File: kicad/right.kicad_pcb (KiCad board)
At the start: 4 copper layers, 127.3 x 89.6 mm, 150 parts, among them Q1 PMF170XP,115, Q2 FS8205A_C2830320, SW1 TS-1088-AR02016, U1 TLV7031QDCKRQ1, U2 E73-2G4M08S1C, U3 SN74LVC1G74DQER, U4 BL8573CS8TR, U6 S2B-PH-K-S(LF)(SN), U7 LP5024RSMR, U8 DW01A_C42380662, X1 FC-13532.768KHZ9PF20PPM

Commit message: added fiducials
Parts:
- added ?: , , F.Cu at (25.4, 113.4)
- added ?: , , B.Cu at (25.4, 113.4)
- added ?: , , B.Cu at (152.4, 49.0)
- added ?: , , B.Cu at (25.4, 49.0)
- added REF**: Fiducial_1mm_Mask2mm, Fiducial:Fiducial_1mm_Mask2mm, F.Cu at (152.4, 49.0)
- added REF**: Fiducial_1mm_Mask2mm, Fiducial:Fiducial_1mm_Mask2mm, F.Cu at (25.4, 49.0)
- moved G** 261.5 mm to (370.8, 131.0)
- moved G*** 237.1 mm to (390.8, -23.2)
- moved G*** 237.1 mm to (401.2, 64.9)
- moved Battery? 71.2 mm to (58.6, 75.3)
- moved C6 71.2 mm to (145.7, 42.9)
- moved C7 71.2 mm to (145.7, 64.4)
- moved C8 71.2 mm to (145.7, 85.9)
- moved D2 71.2 mm to (152.8, 51.1)
- moved D3 71.2 mm to (152.8, 72.6)
- moved D4 71.2 mm to (152.8, 94.1)
- moved D5 71.2 mm to (134.0, 40.3)
- moved D6 71.2 mm to (134.0, 61.8)
- moved D7 71.2 mm to (134.0, 83.3)
- moved hex_edge 71.2 mm to (144.6, 91.9)
- moved hex_edge 71.2 mm to (144.6, 48.9)
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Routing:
- net /D+: track 77.8 -> 71.3 mm
- net /D-: track 73.1 -> 69.0 mm
- net /LED20: track 43.9 -> 45.7 mm

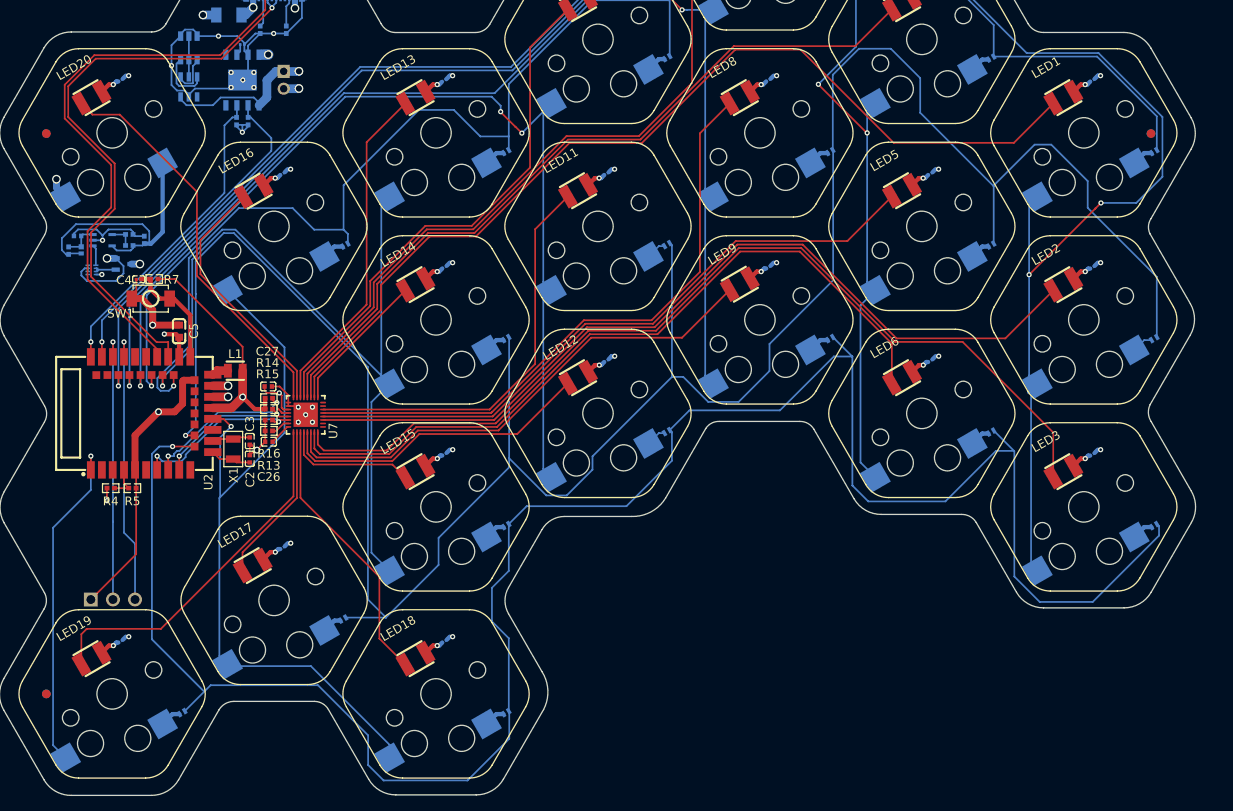
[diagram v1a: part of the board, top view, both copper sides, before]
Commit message: added mounting holes
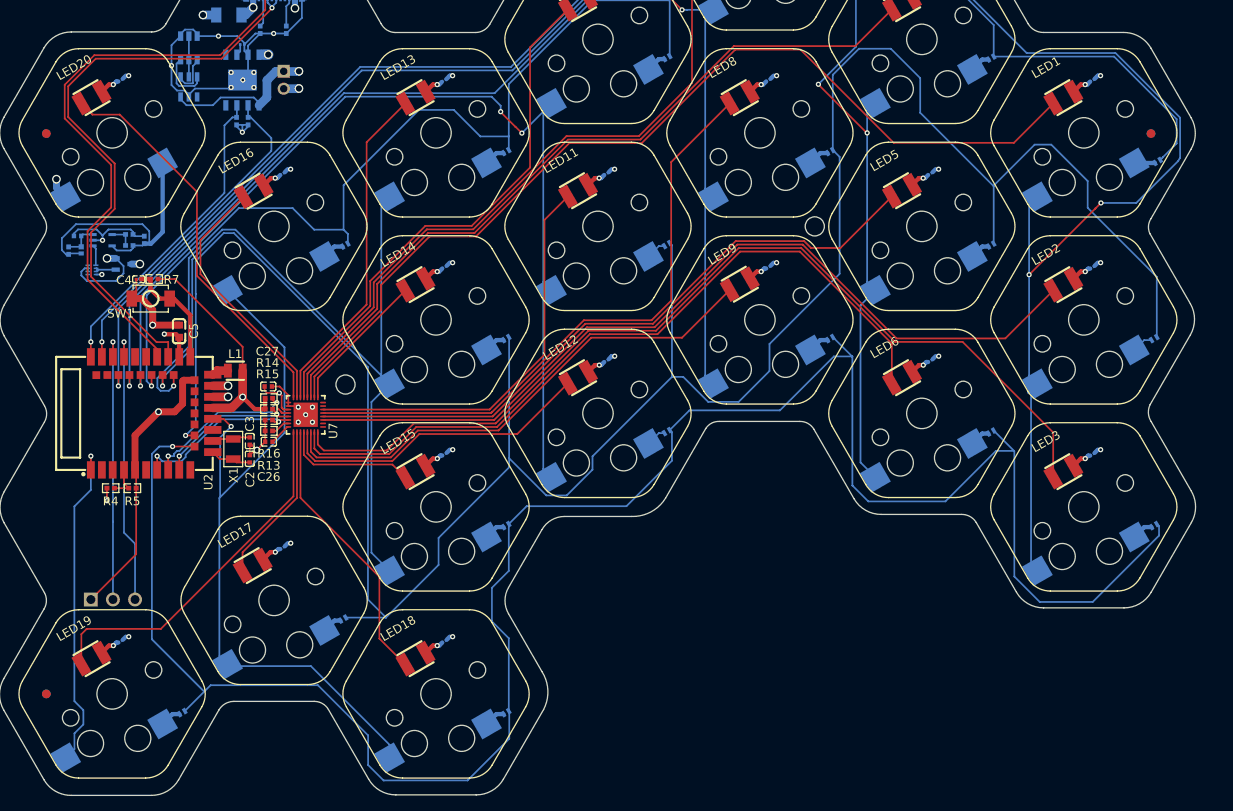
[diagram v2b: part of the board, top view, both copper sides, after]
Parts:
- added ?: , , F.Cu at (59.8, 77.8)
- added M2: MountingHole_2.2mm_M2, MountingHole:MountingHole_2.2mm_M2, F.Cu at (113.8, 59.7)
- Fi1, Fi2, Fi3, Fi6: renamed from ?; value (none) -> Fiducial_1mm_Mask2mm
- moved D2 1.20 mm to (153.2, 52.2)
- renumbered REF** to Fi4, REF** to Fi5
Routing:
- net /ROW1: track 183.0 -> 187.0 mm
- net /COL1: track 230.7 -> 233.5 mm
- net /LED5: track 75.9 -> 76.5 mm
- net /ROW2: track 286.0 -> 286.6 mm

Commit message: changed mounting holes. cleared a little bit, created 21 key version... needs 21 key integration
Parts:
- removed the ? at (59.8, 77.8)
- removed the S12 at (88.9, 102.7)
- added REF**: MountingHole_2.2mm_M2, MountingHole:MountingHole_2.2mm_M2, F.Cu at (57.8, 38.2)
- added REF**: MountingHole_2.2mm_M2, MountingHole:MountingHole_2.2mm_M2, F.Cu at (40.7, 91.9)
- added hex_edge: , clipboard:b9cf7df6-7b49-4194-bf11-16aaca528749, F.Cu at (88.9, 102.7)
- moved G*** 500.2 mm to (-106.6, 29.5)
- moved G*** 500.2 mm to (-96.2, 117.5)
- moved G** 375.1 mm to (38.5, -42.9)
- moved Q2 3.01 mm to (44.7, 39.9)
- moved U8 3.01 mm to (44.7, 44.4)
- moved U6 2.99 mm to (55.6, 43.6)
- moved R10 1.90 mm to (49.7, 39.5)
- moved R12 1.90 mm to (50.3, 48.3)
- moved R11 1.90 mm to (49.0, 48.3)
- moved U4 1.90 mm to (49.7, 43.6)
- moved L1 1.69 mm to (46.1, 74.9)
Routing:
- net /PWR: track 65.7 -> 106.7 mm, vias 24 -> 25
- net /ROW3: track 238.5 -> 203.3 mm, vias 1 -> 7
- net GND: track 148.3 -> 125.3 mm, vias 42 -> 43
- net /VDD_nRF: track 74.9 -> 52.4 mm
- net /BAT+: track 84.3 -> 67.8 mm, vias 3 -> 2
- net /COL5: track 94.2 -> 103.2 mm
- net /VBUS: track 69.1 -> 62.7 mm
- net /COL6: track 84.3 -> 80.2 mm
- net /ROW2: track 286.6 -> 289.8 mm
- net /COL7: track 38.3 -> 35.2 mm
- net /COL4: track 116.1 -> 118.3 mm
- net /COL3: track 138.2 -> 140.3 mm
- net /COL2: track 183.8 -> 185.8 mm
- net /LED16: track 29.7 -> 28.1 mm
- net /PWR_BTN: track 31.4 -> 29.8 mm
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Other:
- outline, holes or cut-outs redrawn

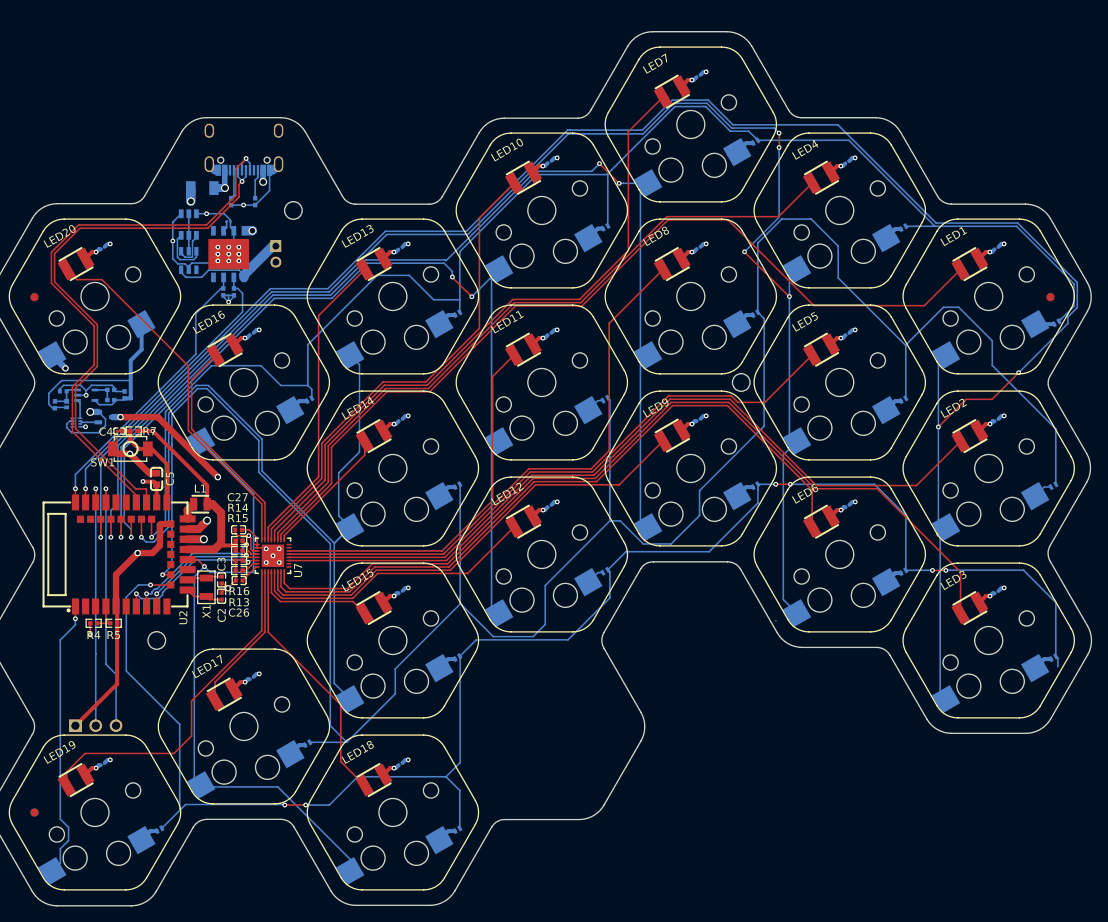
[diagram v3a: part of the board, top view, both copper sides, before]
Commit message: integrated the move from distant index to lowest index... changed from 7colX3row to 5colX4row
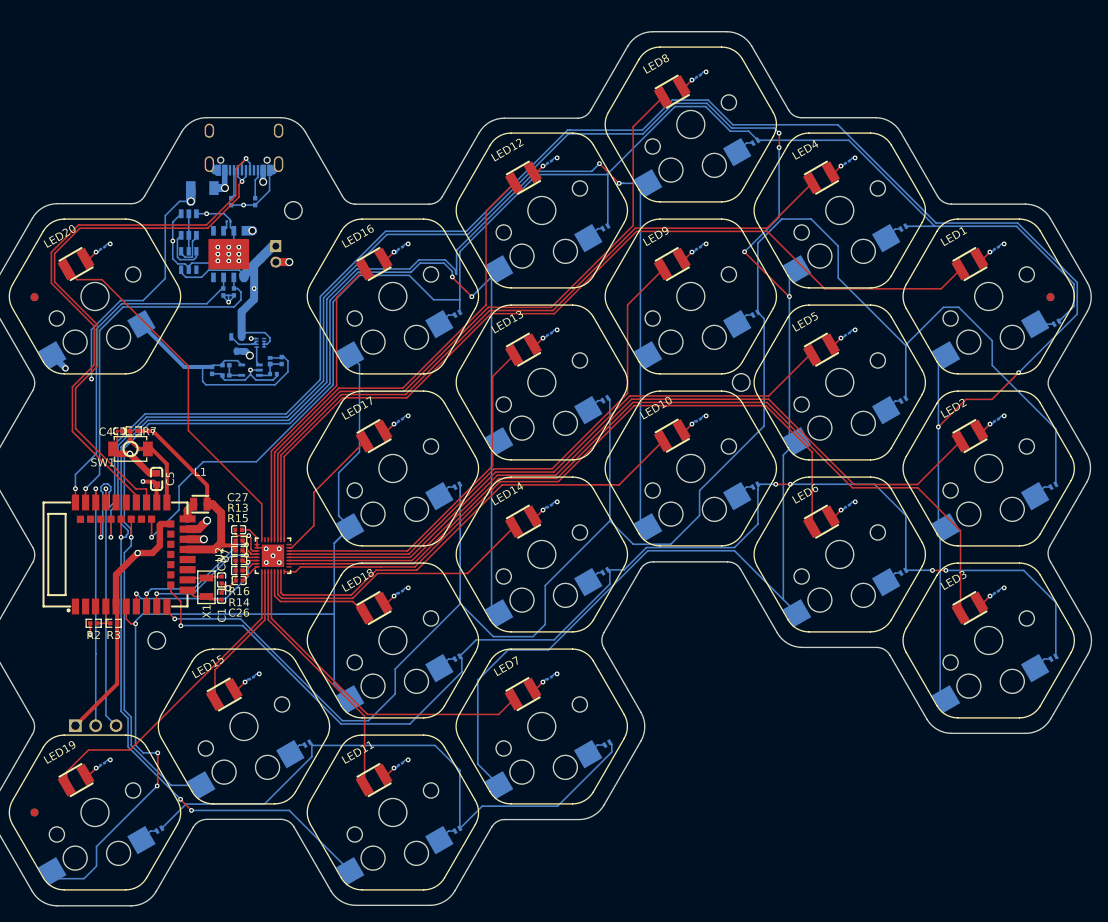
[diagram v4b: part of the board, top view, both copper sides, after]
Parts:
- removed the C1 at (29.0, 60.8)
- removed the R2 at (28.0, 62.5)
- removed the R3 at (35.0, 60.6)
- added C2: GRM155Z71A105KE01D, easyeda2kicad:C0402, B.Cu at (55.3, 58.6)
- added R4: WR04W2494FTL, easyeda2kicad:R0402, B.Cu at (56.3, 56.9)
- added R5: RC0402FR-074M3L, easyeda2kicad:R0402, B.Cu at (49.3, 58.8)
- moved LED7 77.6 mm to (86.5, 98.6)
- moved LED11 57.0 mm to (67.9, 109.4)
- moved D8 56.9 mm to (97.0, 104.8)
- moved S7 56.9 mm to (88.8, 102.7)
- moved C9 56.9 mm to (89.8, 96.6)
- moved LED12 43.0 mm to (86.5, 34.1)
- moved LED17 37.3 mm to (67.9, 66.4)
- moved LED10 37.2 mm to (105.1, 66.3)
- moved D1 26.0 mm to (54.9, 57.0), turned to -90 degrees
- moved U3 25.1 mm to (53.6, 54.7), turned to 90 degrees
- moved D12 21.6 mm to (78.3, 115.6)
- moved D16 21.6 mm to (59.5, 104.8)
- moved LED15 21.6 mm to (49.1, 98.7)
- moved LED8 21.6 mm to (105.1, 23.3)
- moved LED14 21.5 mm to (86.5, 77.1)
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- renumbered C2 to C1, D9 to D10, D10 to D11, D18 to D12, D11 to D13, D12 to D14, D13 to D15, D19 to D16, D14 to D17, D15 to D18, D16 to D19, D17 to D8, D8 to D9, R14 to R13, R13 to R14, R4 to R2, R5 to R3, S9 to S10, S17 to S11, S10 to S12, S11 to S13, S12 to S14, S18 to S15, S13 to S16, S14 to S17, S15 to S18, S16 to S7, S7 to S8, S8 to S9, U6 to U4
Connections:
- D12 pad 2: /ROW2 -> /ROW4
- D16 pad 2: /ROW3 -> /ROW4
- D20 pad 2: /ROW3 -> /ROW4
- D8 pad 2: /ROW1 -> /ROW4
- S11 pad 1: /COL6 -> /COL3
- S15 pad 1: /COL6 -> /COL4
- S19 pad 1: /COL7 -> /COL5
- S7 pad 1: /COL6 -> /COL2
- U2 pad 10: unconnected-(U2-AI6-Pad10) -> /ROW2
- U2 pad 14: /ROW2 -> unconnected-(U2-P0.06-Pad14)
- U2 pad 30: /COL5 -> unconnected-(U2-P17-Pad30)
- U2 pad 6: unconnected-(U2-P1.13-Pad6) -> /COL5
- U7 pad 10: unconnected-(U7-OUT9-Pad10) -> /LED3
- U7 pad 13: /LED8 -> /LED9
- U7 pad 14: /LED11 -> /LED13
- U7 pad 15: unconnected-(U7-OUT14-Pad15) -> /LED17
- U7 pad 17: /LED14 -> /LED1
- U7 pad 18: /LED1 -> /LED4
- U7 pad 19: /LED4 -> /LED8
- U7 pad 2: /LED17 -> /LED15
- U7 pad 20: /LED7 -> /LED12
- U7 pad 21: /LED10 -> /LED16
- U7 pad 22: /LED13 -> unconnected-(U7-OUT21-Pad22)
- U7 pad 23: /LED16 -> unconnected-(U7-OUT22-Pad23)
- U7 pad 3: /LED18 -> /LED11
- U7 pad 4: /LED15 -> /LED7
- U7 pad 5: /LED12 -> /LED18
- U7 pad 6: /LED9 -> /LED14
- U7 pad 7: /LED6 -> /LED10
- U7 pad 8: /LED3 -> /LED6
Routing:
- net /COL6: track 80.2 -> 0.00 mm, vias 1 -> 0
- net /ROW4: track 0.00 -> 76.2 mm
- net /COL3: track 140.3 -> 211.7 mm, vias 3 -> 5
- net /COL2: track 185.8 -> 253.5 mm
- net /ROW2: track 289.8 -> 234.1 mm
- net /ROW3: track 203.3 -> 156.1 mm, vias 7 -> 5
- net /COL4: track 118.3 -> 162.0 mm
- net /LED7: track 83.4 -> 41.9 mm
- net /COL7: track 35.2 -> 0.00 mm, vias 1 -> 0
- net /LED12: track 36.4 -> 61.7 mm
- net /LED14: track 16.5 -> 36.3 mm
- net /PWR: track 106.7 -> 87.3 mm, vias 25 -> 24
- net /COL5: track 103.2 -> 120.3 mm, vias 1 -> 3
- net /LED18: track 31.7 -> 15.2 mm
- net /LED11: track 47.4 -> 31.7 mm
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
